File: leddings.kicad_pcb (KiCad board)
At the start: 2 copper layers, 24 parts, among them J2 Conn_01x04, J3 Micro USB, Q1 FQP30N06L, Q2 FQP30N06L, Q3 FQP30N06L, SW1 SW_RESET, SW2 Boot SEL, U1 LM1117-3.3, U2 CH340G, U3 ESP-07v2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

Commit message: Did a stuff
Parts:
- added J1: TEST_1P, Measurement_Points:Measurement_Point_Square-SMD-Pad_Small, F.Cu at (165.1, 55.9)
- added J4: Conn_01x04, Pin_Headers:Pin_Header_Straight_1x04_Pitch2.54mm, F.Cu at (152.4, 29.2)
- added J5: Micro USB, Connectors_USB:USB_Micro-B_Molex-105017-0001, F.Cu at (161.3, 105.7)
- added J6: Barrel_Jack, Connectors:Barrel_Jack_CUI_PJ-102AH, F.Cu at (142.2, 94.0)
- added MK1: Mounting_Hole, Mounting_Holes:MountingHole_3.2mm_M3_DIN965_Pad, F.Cu at (175.3, 29.2)
- added MK2: Mounting_Hole, Mounting_Holes:MountingHole_3.2mm_M3_DIN965_Pad, F.Cu at (132.1, 104.1)
- added MK3: Mounting_Hole, Mounting_Holes:MountingHole_3.2mm_M3_DIN965_Pad, F.Cu at (132.1, 29.2)
- added MK4: Mounting_Hole, Mounting_Holes:MountingHole_3.2mm_M3_DIN965_Pad, F.Cu at (175.3, 104.1)
- added REF**: Symbol_Barrel_Polarity, Symbols:Symbol_Barrel_Polarity, F.Cu at (153.7, 101.6)
- added REF***: OSHW-Logo_11.4x12mm_SilkScreen, Symbols:OSHW-Logo_11.4x12mm_SilkScreen, B.Cu at (161.3, 86.4)
- J2: value Conn_01x04 -> TEST_1P; footprint Pin_Headers:Pin_Header_Straight_1x04_Pitch2.54mm -> Measurement_Points:Measurement_Point_Square-SMD-Pad_Small
- J3: value Micro USB -> TEST_1P; footprint Connectors_USB:USB_Micro-B_Molex-105017-0001 -> Measurement_Points:Measurement_Point_Square-SMD-Pad_Small
- SW2: footprint Connectors:GS3 -> Pin_Headers:Pin_Header_Straight_1x03_Pitch1.27mm
- U2: footprint Housings_SOIC:HTSOP-8-1EP_3.9x4.9mm_Pitch1.27mm -> Housings_SOIC:SOIC-16_3.9x9.9mm_Pitch1.27mm
- U3: value ESP-07v2 -> ESP-12E; footprint RF_Modules:ESP-12E -> ESP8266:ESP-12E_SMD
- Y1: footprint Crystals:Crystal_HC35-U -> Crystals:Crystal_HC49-U_Vertical
- moved Q3 133.6 mm to (144.8, 43.2), turned to 90 degrees
- moved Q1 124.9 mm to (165.1, 43.2), turned to 90 degrees
- moved J3 113.2 mm to (144.8, 55.9), turned to 0 degrees
- moved Q2 112.5 mm to (154.9, 43.2), turned to 90 degrees
- moved U1 96.2 mm to (134.0, 76.2)
- moved J2 92.9 mm to (154.9, 55.9)
- moved R6 82.9 mm to (149.9, 40.6), turned to 90 degrees
- moved SW1 82.3 mm to (133.8, 70.5), turned to 90 degrees
- moved U2 74.3 mm to (161.3, 94.0), turned to 180 degrees
- moved SW2 73.7 mm to (149.9, 78.7)
- moved R4 73.1 mm to (170.2, 40.7), turned to 90 degrees
- moved C3 64.1 mm to (168.9, 92.7), turned to 270 degrees
- moved Y1 62.8 mm to (172.7, 91.2), turned to 90 degrees
- moved U3 61.0 mm to (168.9, 63.5), turned to 270 degrees
- moved R5 56.8 mm to (160.0, 41.4), turned to 270 degrees
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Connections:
- J2 pad 1: /LED Driver/GreenChannel -> /Controller/BLUE
- J3 pad 1: VBUS -> /Controller/GREEN
- Q2 pad 2: /LED Driver/GreenChannel -> /LED Driver/BlueChannel
- Q3 pad 2: /LED Driver/BlueChannel -> /LED Driver/GreenChannel
- R2 pad 2: /Controller/GREEN -> /Controller/BLUE
- R3 pad 2: /Controller/BLUE -> /Controller/GREEN
- U2 pad 5: Net-(J3-Pad3) -> Net-(J5-Pad3)
- U2 pad 6: Net-(J3-Pad2) -> Net-(J5-Pad2)
- U3 pad 17: (no net) -> Net-(U3-Pad17)
- U3 pad 18: (no net) -> Net-(U3-Pad18)
- U3 pad 19: (no net) -> Net-(U3-Pad19)
- U3 pad 20: (no net) -> Net-(U3-Pad20)
- U3 pad 21: (no net) -> Net-(U3-Pad21)
- U3 pad 22: (no net) -> Net-(U3-Pad22)
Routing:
- net +12V: track 0.00 -> 100.6 mm
- net VCC: track 0.00 -> 87.7 mm, vias 0 -> 3
- net /Controller/RESET: track 0.00 -> 83.8 mm, vias 0 -> 4
- net /Controller/BOOT_SELECT: track 0.00 -> 36.7 mm
- net /Controller/RX: track 0.00 -> 25.0 mm, vias 0 -> 2
- net /Controller/GREEN: track 0.00 -> 23.4 mm, vias 0 -> 2
- net /USB UART Interface/RX: track 0.00 -> 23.1 mm, vias 0 -> 2
- net /LED Driver/GreenChannel: track 0.00 -> 15.3 mm
- net /LED Driver/RedChannel: track 0.00 -> 15.3 mm
- net /Controller/BLUE: track 0.00 -> 14.4 mm
- net /LED Driver/BlueChannel: track 0.00 -> 14.3 mm
- net Net-(J5-Pad2): track 0.00 -> 13.5 mm
- net /Controller/RED: track 0.00 -> 13.0 mm
- net VBUS: track 0.00 -> 12.8 mm
- net Net-(Q2-Pad1): track 0.00 -> 12.8 mm
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- added copper zone on B.Cu, net GND
- added copper zone on F.Cu, net GND
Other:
- board outline added: 50.8 x 82.6 mm
- net class Default: via_dia 0.6 -> 0.8
- rule pad_to_mask_clearance: 0.2 -> 0
- board text added: "+"
- board text added: "-"
- board text added: "12V 2A"
- board text added: "300 LEDs"
- board text added: "Alexander Schramm Wifi RGB Driver July 2018 v1.0"
- board text added: "G B R 12V"

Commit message: ??
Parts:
- moved R6 6.35 mm to (143.5, 40.6)
- moved Q3 6.35 mm to (138.4, 43.2)
- moved R3 6.35 mm to (138.4, 50.9)
- moved J3 2.84 mm to (142.2, 54.6)
- moved R5 2.64 mm to (157.5, 40.6), turned to 90 degrees
- moved Q2 2.54 mm to (152.4, 43.2)
- moved R2 2.54 mm to (152.4, 50.9)
- moved J2 1.80 mm to (156.2, 54.6)
- moved R7 1.27 mm to (143.5, 63.5), turned to 90 degrees
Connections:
- U3 pad 6: /Controller/GREEN -> /Controller/BLUE
- U3 pad 7: /Controller/BLUE -> /Controller/GREEN
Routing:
- net +12V: track 100.6 -> 88.5 mm
- net /Controller/RESET: track 83.8 -> 77.3 mm, vias 4 -> 3
- net /LED Driver/GreenChannel: track 15.3 -> 21.7 mm
- net GND: track 6.41 -> 4.25 mm
- net /Controller/GREEN: track 23.4 -> 25.0 mm, vias 2 -> 0
- net /LED Driver/BlueChannel: track 14.3 -> 13.2 mm
- net Net-(Q2-Pad1): track 12.8 -> 12.0 mm
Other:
- board text added: "Alexander Schramm Wifi RGB Driver Oct 2018 v1.0"
- board text removed: "Alexander Schramm Wifi RGB Driver July 2018 v1.0"

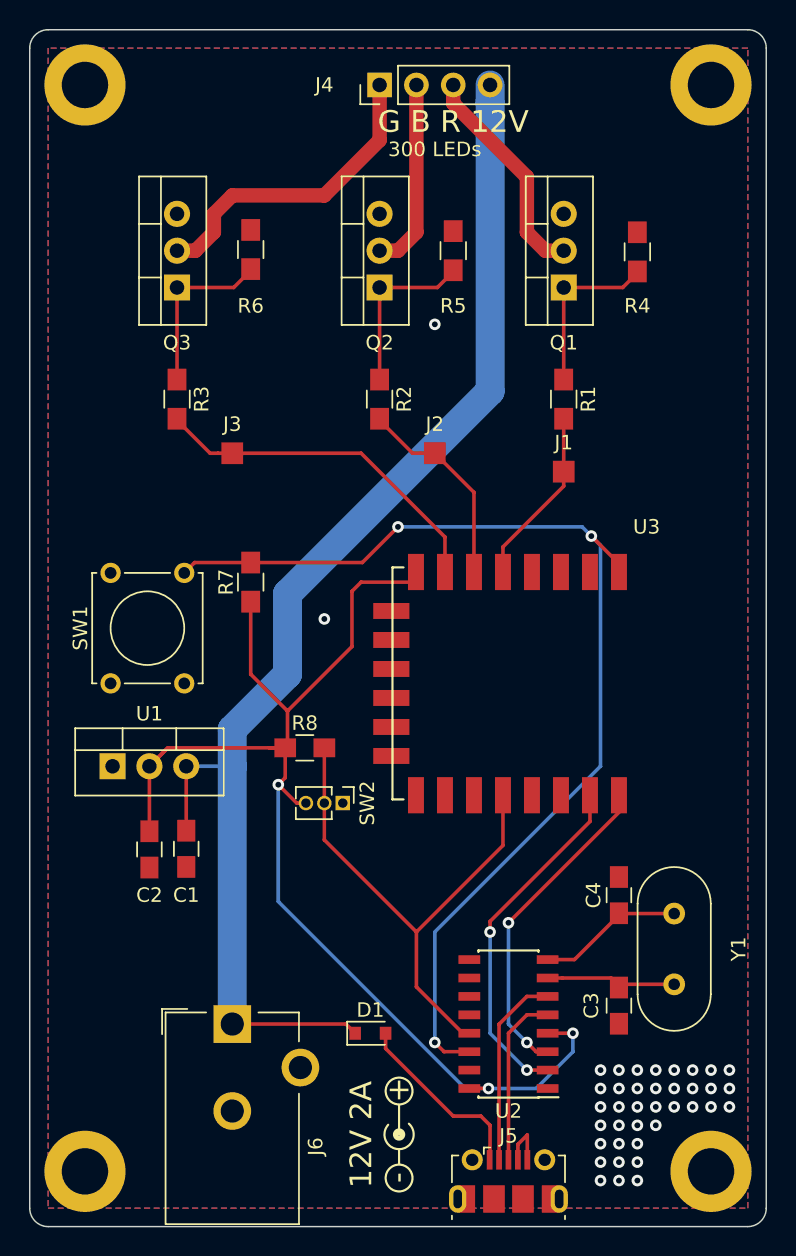
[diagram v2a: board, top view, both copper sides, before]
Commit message: added pin headers for uart, added power-on-led, improved routing
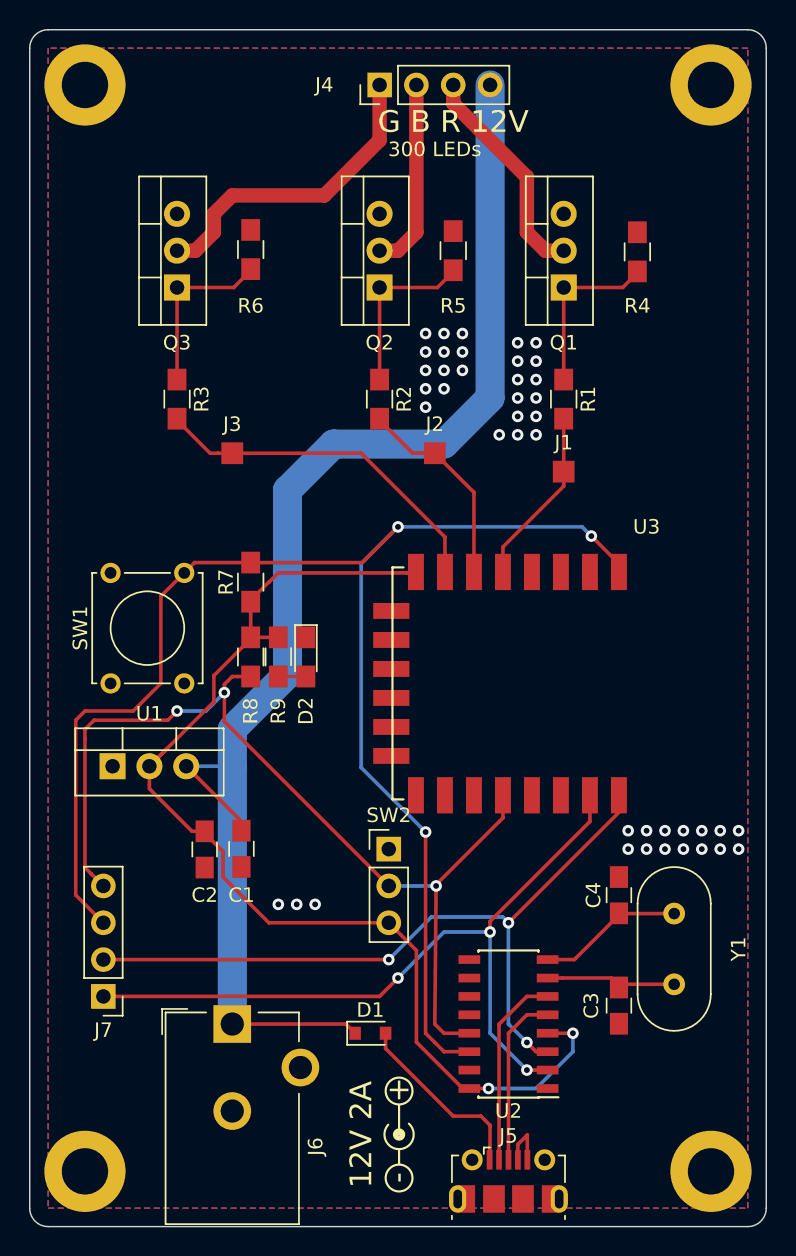
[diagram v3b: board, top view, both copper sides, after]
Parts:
- added D2: LED, LEDs:LED_0805_HandSoldering, F.Cu at (147.3, 68.7)
- added J7: Conn_01x04, Pin_Headers:Pin_Header_Straight_1x04_Pitch2.54mm, F.Cu at (133.3, 92.1)
- added R9: R, Resistors_SMD:R_0805_HandSoldering, F.Cu at (145.4, 68.7)
- SW2: footprint Pin_Headers:Pin_Header_Straight_1x03_Pitch1.27mm -> Pin_Headers:Pin_Header_Straight_1x03_Pitch2.54mm
- moved R8 7.30 mm to (143.5, 68.7), turned to 270 degrees
- moved SW2 4.49 mm to (153.0, 81.9), turned to 0 degrees
- moved C1 3.81 mm to (142.9, 81.9)
- moved C2 3.81 mm to (140.3, 81.9)
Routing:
- net /Controller/BOOT_SELECT: track 36.7 -> 68.6 mm, vias 0 -> 3
- net /USB UART Interface/RX: track 23.1 -> 52.4 mm, vias 2 -> 3
- net /Controller/RESET: track 77.3 -> 106.0 mm
- net /Controller/RX: track 25.0 -> 53.5 mm, vias 2 -> 3
- net VCC: track 87.5 -> 78.4 mm, vias 3 -> 2
- net +12V: track 88.5 -> 94.5 mm
- net Net-(D2-Pad2): track 0.00 -> 1.91 mm
- net GND: vias 39 -> 42

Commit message: changed some parts to smd, fixed some design errors
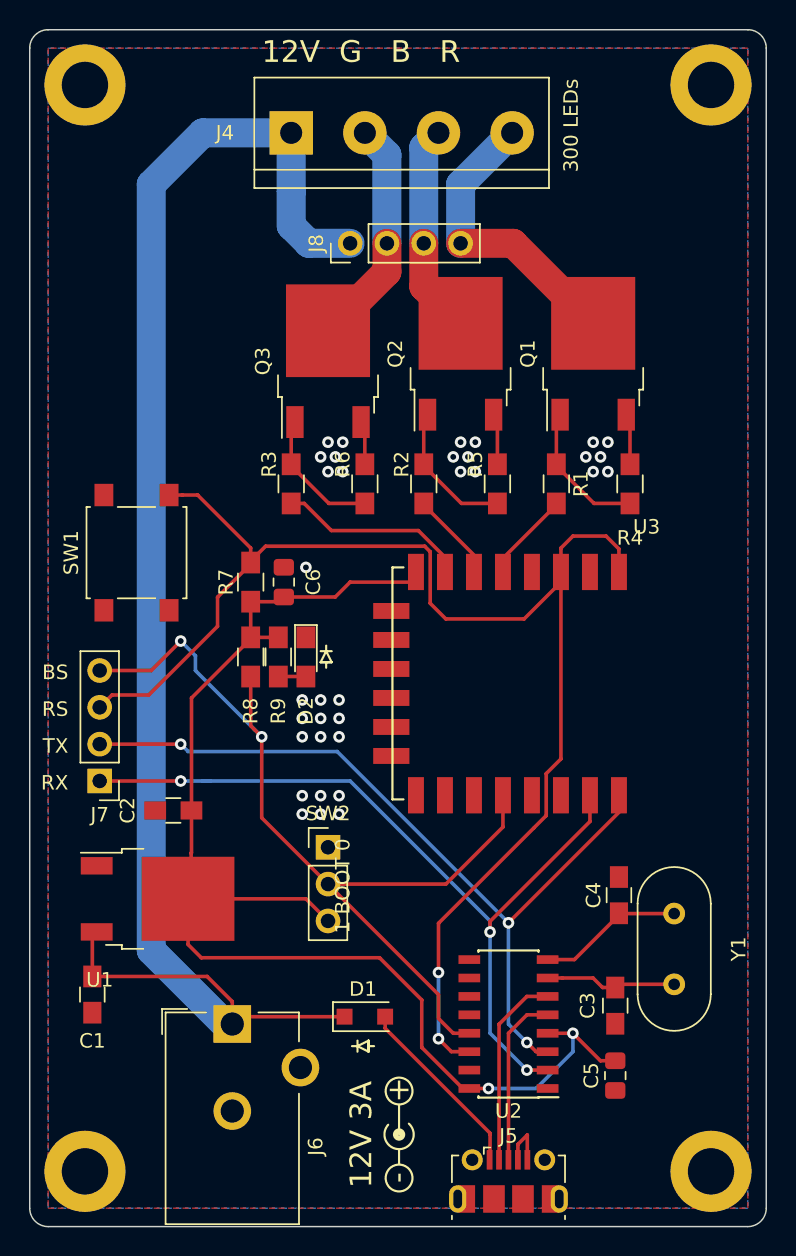
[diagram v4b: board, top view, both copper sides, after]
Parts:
- removed J1, J2, J3: TEST_1P, Measurement_Points:Measurement_Point_Square-SMD-Pad_Small
- added C5: 10uF, Capacitor_SMD:C_0805_2012Metric_Pad1.15x1.40mm_HandSolder, F.Cu at (168.7, 97.5)
- added C6: 10uF, Resistor_SMD:R_0805_2012Metric_Pad1.15x1.40mm_HandSolder, F.Cu at (145.8, 63.5)
- added J8: Conn_01x04, Connector_PinHeader_2.54mm:PinHeader_1x04_P2.54mm_Vertical, F.Cu at (150.4, 40.1)
- added REF**: Diode Symbol, miscparts:Diode Symbol, F.Cu at (148.7, 68.3)
- added REF**: Diode Symbol, miscparts:Diode Symbol, F.Cu at (150.9, 95.5)
- D1: footprint Diodes_SMD:D_0805 -> Diode_SMD:D_SOD-123F
- J4: footprint Pin_Headers:Pin_Header_Straight_1x04_Pitch2.54mm -> TerminalBlock:TerminalBlock_bornier-4_P5.08mm
- Q1, Q2, Q3: value FQP30N06L -> IRLR8726TRLPBF; footprint TO_SOT_Packages_THT:TO-220-3_Vertical -> Package_TO_SOT_SMD:TO-252-2
- R9: value R -> 10K
- SW1: footprint Buttons_Switches_THT:SW_Tactile_Straight_KSA0Axx1LFTR -> Button_Switch_SMD:SW_SPST_B3S-1000
- U1: footprint TO_SOT_Packages_THT:TO-220-3_Vertical -> Package_TO_SOT_SMD:TO-252-2
- moved REF*** 30.5 mm to (152.4, 57.1)
- moved R6 18.0 mm to (151.4, 56.7)
- moved R5 16.4 mm to (160.5, 56.7)
- moved R4 16.0 mm to (169.7, 56.7)
- moved J7 14.9 mm to (133.1, 77.2)
- moved C1 14.4 mm to (132.6, 91.9)
- moved Q3 11.6 mm to (148.8, 48.3)
- moved R3 9.80 mm to (146.3, 56.7)
- moved U1 9.66 mm to (137.1, 85.3)
- moved SW1 9.19 mm to (135.6, 61.5)
- moved Q2 7.22 mm to (158.0, 47.8)
- moved J4 6.93 mm to (146.3, 32.5), turned to 0 degrees
- moved R2 6.59 mm to (155.4, 56.7)
- moved R1 5.86 mm to (164.6, 56.7)
- moved Q1 5.00 mm to (167.1, 47.8)
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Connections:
- J4 pad 1: /LED Driver/GreenChannel -> +12V
- J4 pad 2: /LED Driver/BlueChannel -> /LED Driver/GreenChannel
- J4 pad 3: /LED Driver/RedChannel -> /LED Driver/BlueChannel
- J4 pad 4: +12V -> /LED Driver/RedChannel
- J5 pad 6: (no net) -> GND
- U3 pad 10: Net-(U3-Pad10) -> GND
- U3 pad 3: GND -> /Controller/RESET
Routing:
- net VCC: track 78.4 -> 90.0 mm
- net /Controller/GREEN: track 25.0 -> 13.9 mm
- net +12V: track 94.5 -> 105.7 mm
- net GND: track 4.25 -> 14.2 mm, vias 42 -> 34
- net /Controller/BLUE: track 14.9 -> 7.07 mm
- net /Controller/RED: track 13.0 -> 6.95 mm
- net /Controller/RESET: track 106.0 -> 100.2 mm, vias 3 -> 2
- net /LED Driver/GreenChannel: track 21.7 -> 16.0 mm
- net /LED Driver/RedChannel: track 15.3 -> 20.5 mm
- net /USB UART Interface/RX: track 52.4 -> 56.4 mm
- net /Controller/RX: track 53.5 -> 57.2 mm
- net /Controller/BOOT_SELECT: track 68.6 -> 65.0 mm, vias 3 -> 2
- net Net-(Q3-Pad1): track 12.0 -> 9.28 mm
- net Net-(Q2-Pad1): track 12.0 -> 9.78 mm
- net Net-(Q1-Pad1): track 11.9 -> 9.78 mm
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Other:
- board text added: "1 BOOT 0"
- board text added: "12V 3A"
- board text added: "12V G B R"
- board text added: "BS"
- board text added: "RS"
- board text added: "RX"
- board text added: "TX"
- board text removed: "12V 2A"
- board text removed: "G B R 12V"

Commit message: changed text on pcb
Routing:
- net GND: vias 34 -> 36
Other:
- board text added: "Alexander Schramm Wifi RGB Driver Oct 2018 v1.1"
- board text removed: "Alexander Schramm Wifi RGB Driver Oct 2018 v1.0"
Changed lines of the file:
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@@
     (thickness 1.6)
     (drawings 19)
-    (tracks 248)
+    (tracks 250)
     (zones 0)
     (modules 39)
@@
     (34 B.Paste user)
     (35 F.Paste user)
-    (36 B.SilkS user hide)
+    (36 B.SilkS user)
     (37 F.SilkS user)
     (38 B.Mask user)
@@
       (plotinvisibletext false)
       (padsonsilk false)
-      (subtractmaskfromsilk false)
+      (subtractmaskfromsilk true)
       (outputformat 1)
       (mirror false)
@@
     (effects (font (size 1 1) (thickness 0.2)) (justify right))
   )
-  (gr_text "Alexander Schramm\nWifi RGB Driver\nOct 2018\nv1.0" (at 152.908 69.85) (layer B.SilkS)
+  (gr_text "Alexander Schramm\nWifi RGB Driver\nOct 2018\nv1.1" (at 152.908 69.85) (layer B.SilkS)
     (effects (font (size 1.5 1.5) (thickness 0.3)) (justify mirror))
   )
@@
   (gr_arc (start 129.54 26.67) (end 129.54 25.4) (angle -90) (layer Edge.Cuts) (width 0.1))
   (gr_arc (start 177.8 26.67) (end 179.07 26.67) (angle -90) (layer Edge.Cuts) (width 0.1))
-  (via (at 157.48 54.864) (size 0.8) (drill 0.4) (layers F.Cu B.Cu) (net 2))
-  (via (at 157.988 55.88) (size 0.8) (drill 0.4) (layers F.Cu B.Cu) (net 2))
-  (via (at 149.352 54.864) (size 0.8) (drill 0.4) (layers F.Cu B.Cu) (net 2))
-  (via (at 148.336 54.864) (size 0.8) (drill 0.4) (layers F.Cu B.Cu) (net 2))
-  (segment (start 163.54 98.425) (end 163.99 98.425) (width 0.25) (layer F.Cu) (net 2))
-  (segment (start 162.59 103.345) (end 162.59 101.63) (width 0.25) (layer F.Cu) (net 2))
-  (segment (start 161.94 102.28) (end 161.94 103.345) (width 0.25) (layer F.Cu) (net 2))
-  (segment (start 161.94 102.28) (end 162.59 101.63) (width 0.25) (layer F.Cu) (net 2))
-  (via (at 165.735 94.615) (size 0.8) (drill 0.4) (layers F.Cu B.Cu) (net 3))
-  (segment (start 163.99 94.615) (end 165.735 94.615) (width 0.25) (layer F.Cu) (net 3))
-  (segment (start 165.735 94.615) (end 165.735 95.885) (width 0.25) (layer B.Cu) (net 3))
-  (via (at 159.915 98.425) (size 0.8) (drill 0.4) (layers F.Cu B.Cu) (net 3))
-  (segment (start 165.735 95.885) (end 163.195 98.425) (width 0.25) (layer B.Cu) (net 3))
-  (segment (start 163.195 98.425) (end 159.915 98.425) (width 0.25) (layer B.Cu) (net 3))
-  (segment (start 159.915 98.425) (end 158.59 98.425) (width 0.25) (layer F.Cu) (net 3))
-  (segment (start 143.51 64.85) (end 143.51 64.75) (width 0.25) (layer F.Cu) (net 3))
-  (segment (start 169.13 91.24) (end 168.91 91.46) (width 0.25) (layer F.Cu) (net 4))
-  (segment (start 168.91 91.46) (end 168.91 91.335) (width 0.25) (layer F.Cu) (net 4))
-  (segment (start 168.93 86.36) (end 168.91 86.34) (width 0.25) (layer F.Cu) (net 5))
-  (segment (start 172.72 86.36) (end 168.93 86.36) (width 0.25) (layer F.Cu) (net 5))
-  (segment (start 168.91 86.465) (end 168.91 86.34) (width 0.25) (layer F.Cu) (net 5))
-  (segment (start 165.84 89.535) (end 168.91 86.465) (width 0.25) (layer F.Cu) (net 5))
-  (segment (start 163.99 89.535) (end 165.84 89.535) (width 0.25) (layer F.Cu) (net 5))
-  (segment (start 159.99 102.87) (end 160.02 102.84) (width 0.25) (layer F.Cu) (net 6))
-  (segment (start 159.99 103.345) (end 159.99 102.87) (width 0.25) (layer F.Cu) (net 6))
   (segment (start 142.748 93.472) (end 142.24 93.98) (width 0.25) (layer F.Cu) (net 1))
   (segment (start 149.984 93.472) (end 142.748 93.472) (width 0.25) (layer F.Cu) (net 1))
@@
   (segment (start 132.588 87.928) (end 132.892 87.624) (width 0.25) (layer F.Cu) (net 1))
   (segment (start 132.588 90.698) (end 132.588 87.928) (width 0.25) (layer F.Cu) (net 1))
+  (via (at 157.48 54.864) (size 0.8) (drill 0.4) (layers F.Cu B.Cu) (net 2))
+  (via (at 157.988 55.88) (size 0.8) (drill 0.4) (layers F.Cu B.Cu) (net 2))
+  (via (at 149.352 54.864) (size 0.8) (drill 0.4) (layers F.Cu B.Cu) (net 2))
+  (via (at 148.336 54.864) (size 0.8) (drill 0.4) (layers F.Cu B.Cu) (net 2))
+  (segment (start 163.54 98.425) (end 163.99 98.425) (width 0.25) (layer F.Cu) (net 2))
+  (segment (start 162.59 103.345) (end 162.59 101.63) (width 0.25) (layer F.Cu) (net 2))
+  (segment (start 161.94 102.28) (end 161.94 103.345) (width 0.25) (layer F.Cu) (net 2))
+  (segment (start 161.94 102.28) (end 162.59 101.63) (width 0.25) (layer F.Cu) (net 2))
   (segment (start 151.384 52.72) (end 151.124 52.46) (width 0.25) (layer F.Cu) (net 2))
   (segment (start 151.384 55.372) (end 151.384 52.72) (width 0.25) (layer F.Cu) (net 2))
@@
   (via (at 148.336 79.502) (size 0.8) (drill 0.4) (layers F.Cu B.Cu) (net 2))
   (via (at 149.606 79.502) (size 0.8) (drill 0.4) (layers F.Cu B.Cu) (net 2))
+  (via (at 142.748 80.264) (size 0.8) (drill 0.4) (layers F.Cu B.Cu) (net 2))
+  (via (at 144.78 87.376) (size 0.8) (drill 0.4) (layers F.Cu B.Cu) (net 2))
+  (via (at 165.735 94.615) (size 0.8) (drill 0.4) (layers F.Cu B.Cu) (net 3))
+  (segment (start 163.99 94.615) (end 165.735 94.615) (width 0.25) (layer F.Cu) (net 3))
+  (segment (start 165.735 94.615) (end 165.735 95.885) (width 0.25) (layer B.Cu) (net 3))
+  (via (at 159.915 98.425) (size 0.8) (drill 0.4) (layers F.Cu B.Cu) (net 3))
+  (segment (start 165.735 95.885) (end 163.195 98.425) (width 0.25) (layer B.Cu) (net 3))
+  (segment (start 163.195 98.425) (end 159.915 98.425) (width 0.25) (layer B.Cu) (net 3))
+  (segment (start 159.915 98.425) (end 158.59 98.425) (width 0.25) (layer F.Cu) (net 3))
+  (segment (start 143.51 64.85) (end 143.51 64.75) (width 0.25) (layer F.Cu) (net 3))
   (segment (start 167.631 96.511) (end 168.656 96.511) (width 0.25) (layer F.Cu) (net 3))
   (segment (start 165.735 94.615) (end 167.631 96.511) (width 0.25) (layer F.Cu) (net 3))
@@
   (segment (start 143.51 67.41) (end 143.51 67.31) (width 0.25) (layer F.Cu) (net 3))
   (segment (start 139.426 71.494) (end 143.51 67.41) (width 0.25) (layer F.Cu) (net 3))
+  (segment (start 169.13 91.24) (end 168.91 91.46) (width 0.25) (layer F.Cu) (net 4))
+  (segment (start 168.91 91.46) (end 168.91 91.335) (width 0.25) (layer F.Cu) (net 4))
   (segment (start 168.876 91.24) (end 168.656 91.46) (width 0.25) (layer F.Cu) (net 4))
   (segment (start 172.72 91.24) (end 168.876 91.24) (width 0.25) (layer F.Cu) (net 4))
@@
   (segment (start 167.781 91.46) (end 167.126 90.805) (width 0.25) (layer F.Cu) (net 4))
   (segment (start 168.656 91.46) (end 167.781 91.46) (width 0.25) (layer F.Cu) (net 4))
+  (segment (start 168.93 86.36) (end 168.91 86.34) (width 0.25) (layer F.Cu) (net 5))
+  (segment (start 172.72 86.36) (end 168.93 86.36) (width 0.25) (layer F.Cu) (net 5))
+  (segment (start 168.91 86.465) (end 168.91 86.34) (width 0.25) (layer F.Cu) (net 5))
+  (segment (start 165.84 89.535) (end 168.91 86.465) (width 0.25) (layer F.Cu) (net 5))
+  (segment (start 163.99 89.535) (end 165.84 89.535) (width 0.25) (layer F.Cu) (net 5))
+  (segment (start 159.99 102.87) (end 160.02 102.84) (width 0.25) (layer F.Cu) (net 6))
+  (segment (start 159.99 103.345) (end 159.99 102.87) (width 0.25) (layer F.Cu) (net 6))
   (segment (start 160.02 101.508) (end 160.02 101.6) (width 0.25) (layer F.Cu) (net 6))
   (segment (start 152.784 94.272) (end 160.02 101.508) (width 0.25) (layer F.Cu) (net 6))
